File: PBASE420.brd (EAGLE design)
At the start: 100 x 50 mm, 13 parts, among them J1 DC_2_1MM, SW1 MK-12C02-PB

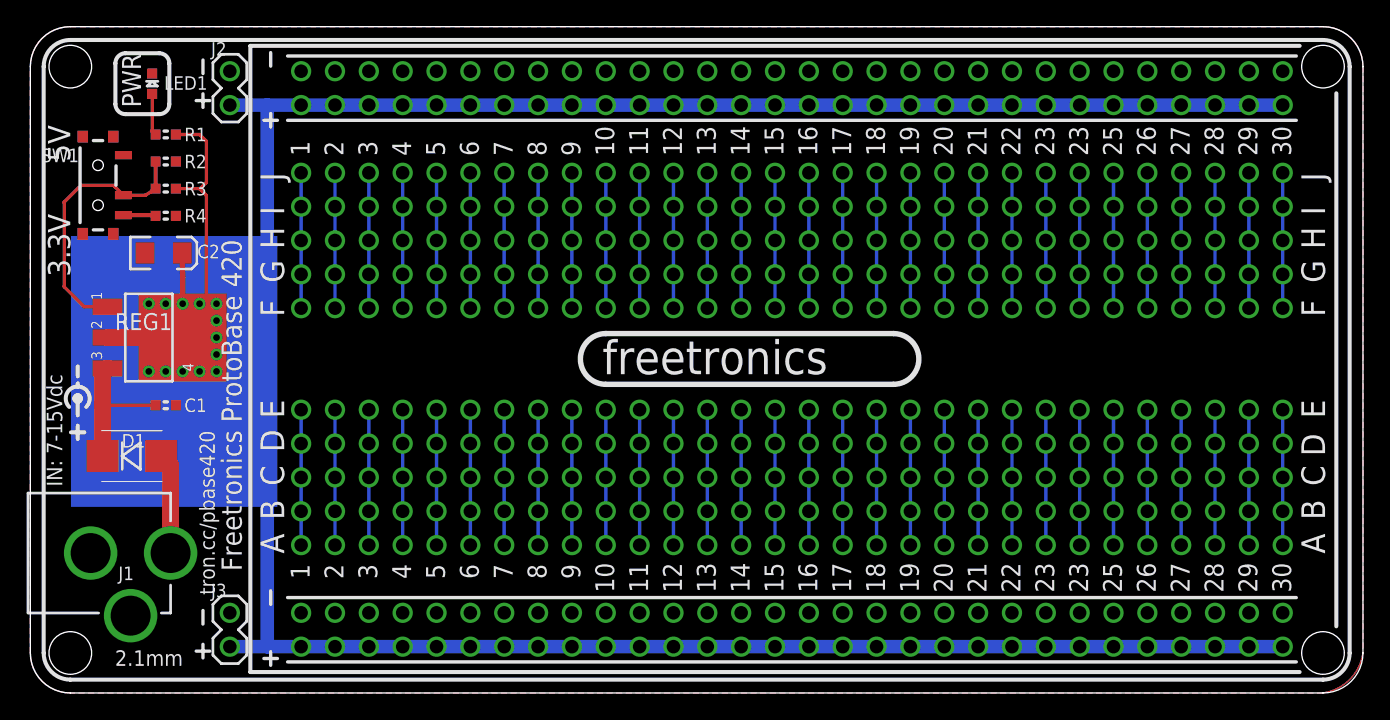
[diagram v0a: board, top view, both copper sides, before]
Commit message: Updated silkscreen, designators, and README
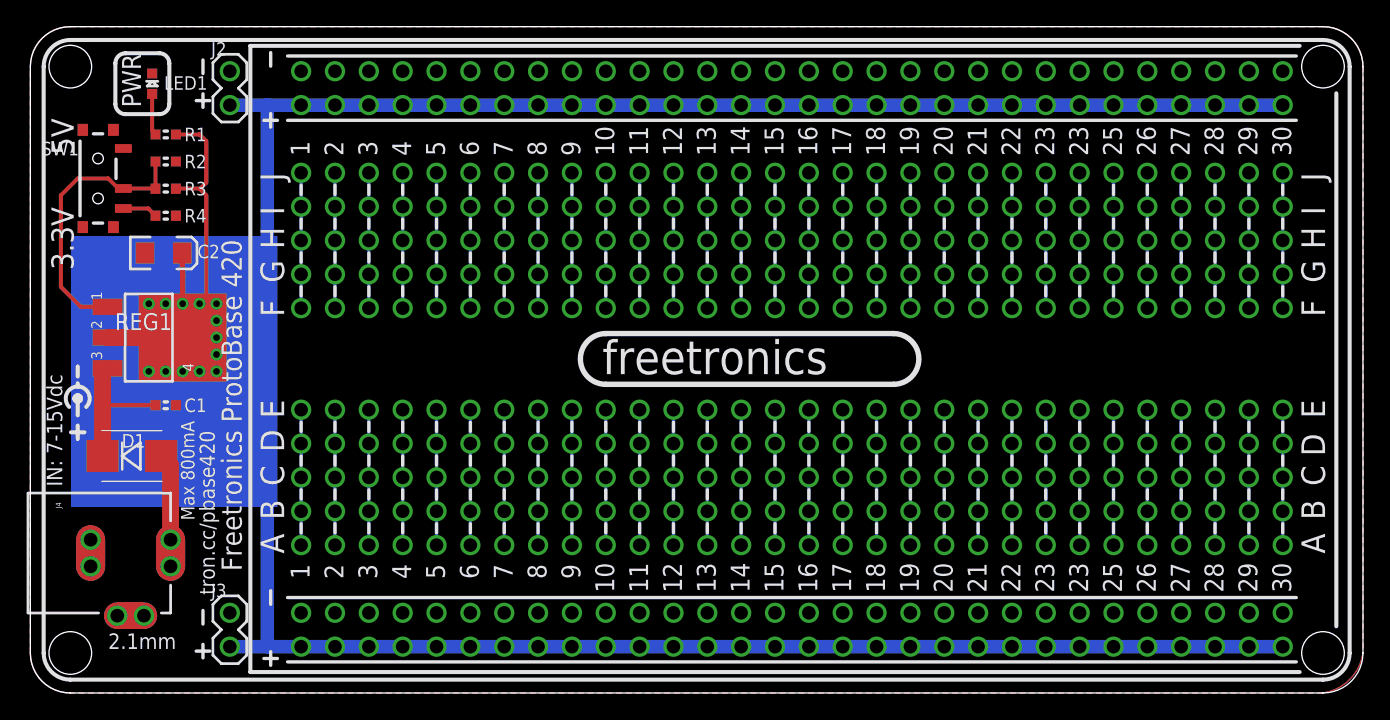
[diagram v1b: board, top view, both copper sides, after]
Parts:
- removed J1: DC_2_1MM, freetronics:POWER_JACK_PTH
- added J4: DC_JACK_2_1PTH, DCJackSlots:FREETRONICS_POWER_JACK_PTH
- C2: value 10uF 6.3V A TANT -> 10uF 10V A TANT
- moved SW1 0.51 mm to (5.08, 38.6)
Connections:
- net GND: now also J4.GND@1, J4.GND@2, J4.GNDBREAK@1, J4.GNDBREAK@2; no longer J1.GND, J1.GNDBREAK
- net N$8: now also J4.PWR@1, J4.PWR@2; no longer J1.PWR
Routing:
- net N$8: track 7.57 -> 6.57 mm
- net N$2: track 20.2 -> 21.0 mm
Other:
- board text added: "Max 800mA"

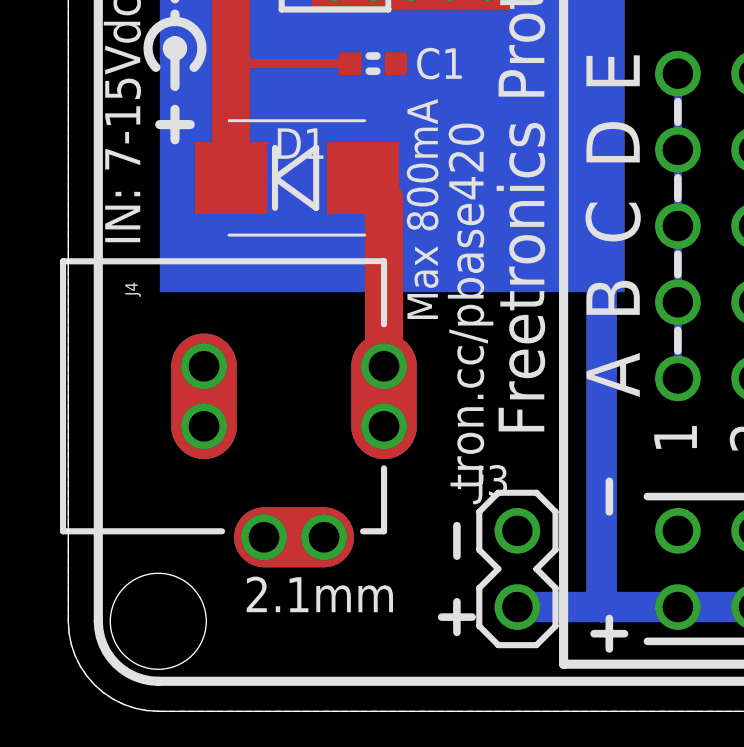
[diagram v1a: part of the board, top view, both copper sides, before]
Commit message: Replaced DC jack footprint with slotted version
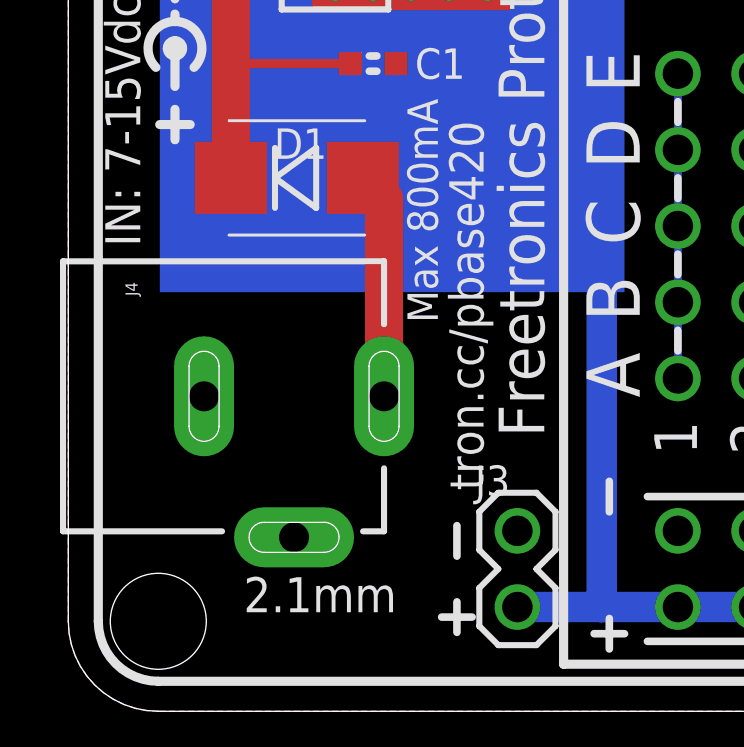
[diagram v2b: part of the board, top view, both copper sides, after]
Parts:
- J4: value DC_JACK_2_1PTH -> POWER_JACKPTH_SLOTS; device DCJackSlots:FREETRONICS_POWER_JACK_PTH -> freetronics-jon:POWER_JACK_PTH_SLOTS
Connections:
- net GND: now also J4.GND, J4.GNDBREAK; no longer J4.GND@1, J4.GND@2, J4.GNDBREAK@1, J4.GNDBREAK@2
- net N$8: now also J4.PWR; no longer J4.PWR@1, J4.PWR@2
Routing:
- net N$8: track 6.57 -> 7.57 mm
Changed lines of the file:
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@@
 <?xml version="1.0" encoding="utf-8"?>
 <!DOCTYPE eagle SYSTEM "eagle.dtd">
-<eagle version="6.5.0">
+<eagle version="8.7.0">
 <drawing>
 <settings>
-<setting alwaysvectorfont="yes"/>
+<setting alwaysvectorfont="no"/>
+<setting keepoldvectorfont="yes"/>
 <setting verticaltext="up"/>
 </settings>
-<grid distance="0.01" unitdist="inch" unit="inch" style="dots" multiple="1" display="yes" altdistance="0.005" altunitdist="inch" altunit="inch"/>
+<grid distance="0.05" unitdist="inch" unit="inch" style="dots" multiple="1" display="yes" altdistance="0.005" altunitdist="inch" altunit="inch"/>
 <layers>
 <layer number="1" name="Top" color="4" fill="1" visible="yes" active="yes"/>
@@
 <layer number="54" name="bGND_GNDA" color="1" fill="9" visible="no" active="no"/>
 <layer number="56" name="wert" color="7" fill="1" visible="no" active="yes"/>
+<layer number="57" name="tCAD" color="7" fill="1" visible="no" active="no"/>
+<layer number="59" name="tCarbon" color="7" fill="1" visible="no" active="no"/>
 <layer number="60" name="p_dimension" color="6" fill="0" visible="no" active="no"/>
 <layer number="61" name="pt_docu" color="7" fill="0" visible="no" active="no"/>
+<layer number="88" name="SimResults" color="9" fill="1" visible="no" active="no"/>
+<layer number="89" name="SimProbes" color="9" fill="1" visible="no" active="no"/>
+<layer number="90" name="Modules" color="7" fill="1" visible="no" active="no"/>
 <layer number="91" name="Nets" color="2" fill="1" visible="no" active="no"/>
 <layer number="92" name="Busses" color="1" fill="1" visible="no" active="no"/>
@@
 <layer number="97" name="Info" color="7" fill="1" visible="no" active="no"/>
 <layer number="98" name="Guide" color="6" fill="1" visible="no" active="no"/>
+<layer number="99" name="SpiceOrder" color="7" fill="1" visible="no" active="no"/>
 <layer number="100" name="Muster" color="7" fill="1" visible="no" active="no"/>
 <layer number="101" name="Patch_Top" color="12" fill="4" visible="no" active="yes"/>
@@
 <layer number="111" name="LPC17xx" color="7" fill="1" visible="yes" active="yes"/>
 <layer number="112" name="tSilk" color="7" fill="1" visible="yes" active="yes"/>
+<layer number="113" name="ReferenceLS" color="7" fill="1" visible="no" active="no"/>
 <layer number="116" name="Patch_BOT" color="9" fill="4" visible="no" active="yes"/>
 <layer number="118" name="Rect_Pads" color="7" fill="1" visible="yes" active="yes"/>
@@
 <layer number="127" name="_tValues" color="7" fill="1" visible="yes" active="yes"/>
 <layer number="128" name="_bValues" color="7" fill="1" visible="yes" active="yes"/>
+<layer number="129" name="Mask" color="7" fill="1" visible="yes" active="yes"/>
 <layer number="131" name="tAdjust" color="7" fill="1" visible="yes" active="yes"/>
 <layer number="132" name="bAdjust" color="7" fill="1" visible="yes" active="yes"/>
@@
 <layer number="146" name="p_Milling" color="3" fill="9" visible="yes" active="yes"/>
 <layer number="147" name="COVER" color="14" fill="1" visible="yes" active="yes"/>
+<layer number="150" name="Notes" color="7" fill="1" visible="yes" active="yes"/>
 <layer number="151" name="HeatSink" color="7" fill="1" visible="no" active="yes"/>
 <layer number="152" name="_bDocu" color="7" fill="1" visible="yes" active="yes"/>
+<layer number="153" name="FabDoc1" color="6" fill="1" visible="no" active="no"/>
+<layer number="154" name="FabDoc2" color="2" fill="1" visible="no" active="no"/>
+<layer number="155" name="FabDoc3" color="7" fill="15" visible="no" active="no"/>
 <layer number="190" name="Comments" color="12" fill="1" visible="yes" active="yes"/>
 <layer number="199" name="Contour" color="7" fill="1" visible="yes" active="yes"/>
@@
 <layer number="223" name="223bmp" color="7" fill="1" visible="no" active="yes"/>
 <layer number="224" name="224bmp" color="7" fill="1" visible="no" active="yes"/>
+<layer number="225" name="225bmp" color="7" fill="1" visible="yes" active="yes"/>
+<layer number="226" name="226bmp" color="7" fill="1" visible="yes" active="yes"/>
+<layer number="227" name="227bmp" color="7" fill="1" visible="yes" active="yes"/>
+<layer number="228" name="228bmp" color="7" fill="1" visible="yes" active="yes"/>
+<layer number="229" name="229bmp" color="7" fill="1" visible="yes" active="yes"/>
+<layer number="230" name="230bmp" color="7" fill="1" visible="yes" active="yes"/>
 <layer number="231" name="Eagle3D_PG1" color="7" fill="1" visible="yes" active="yes"/>
 <layer number="232" name="Eagle3D_PG2" color="7" fill="1" visible="yes" active="yes"/>
@@
 <layer number="251" name="SMDround" color="12" fill="11" visible="no" active="no"/>
 <layer number="254" name="cooling" color="7" fill="1" visible="no" active="yes"/>
+<layer number="255" name="routoute" color="7" fill="1" visible="yes" active="yes"/>
 </layers>
 <board>
@@
 <param name="dpMaxLengthDifference" value="10mm"/>
 <param name="dpGapFactor" value="2.5"/>
-<param name="checkGrid" value="0"/>
 <param name="checkAngle" value="0"/>
 <param name="checkFont" value="1"/>
 <param name="checkRestrict" value="1"/>
+<param name="checkStop" value="0"/>
+<param name="checkValues" value="0"/>
 <param name="useDiameter" value="13"/>
 <param name="maxErrors" value="50"/>
@@
 <pass name="Default">
 <param name="RoutingGrid" value="50mil"/>
+<param name="AutoGrid" value="1"/>
+<param name="Efforts" value="0"/>
+<param name="TopRouterVariant" value="1"/>
 <param name="tpViaShape" value="round"/>
 <param name="PrefDir.1" value="|"/>
@@
 <attribute name="VALUE" x="15.488" y="32.57" size="1.016" layer="27"/>
 </element>
-<element name="J4" library="DCJackSlots" package="FREETRONICS_POWER_JACK_PTH" value="DC_JACK_2_1PTH" x="-3.175" y="10.5" rot="R270"/>
+<element name="J4" library="freetronics-jon" package="POWER_JACK_PTH_SLOTS" value="POWER_JACKPTH_SLOTS" x="-3.175" y="10.5" rot="R270"/>
 </elements>
 <signals>
@@
 <contactref element="R2" pad="2"/>
 <contactref element="R4" pad="2"/>
-<contactref element="J4" pad="GND@2"/>
-<contactref element="J4" pad="GND@1"/>
-<contactref element="J4" pad="GNDBREAK@2"/>
-<contactref element="J4" pad="GNDBREAK@1"/>
+<contactref element="J4" pad="GND"/>
+<contactref element="J4" pad="GNDBREAK"/>
 </signal>
 <signal name="VIN">
@@
 <contactref element="D1" pad="A"/>
 <wire x1="10.525" y1="17.075" x2="9.82" y2="17.78" width="1.27" layer="1"/>
-<contactref element="J4" pad="PWR@2"/>
-<contactref element="J4" pad="PWR@1"/>
-<wire x1="10.525" y1="17.075" x2="10.525" y2="11.5" width="1.27" layer="1"/>
+<contactref element="J4" pad="PWR"/>
+<wire x1="10.525" y1="17.075" x2="10.525" y2="10.5" width="1.27" layer="1"/>
 </signal>
 <signal name="NL1">
@@
 </signal>
 </signals>
-<errors>
-</errors>
 </board>
 </drawing>
